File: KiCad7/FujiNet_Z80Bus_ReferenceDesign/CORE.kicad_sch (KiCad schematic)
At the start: 19 parts, among them IC1 74HC32N

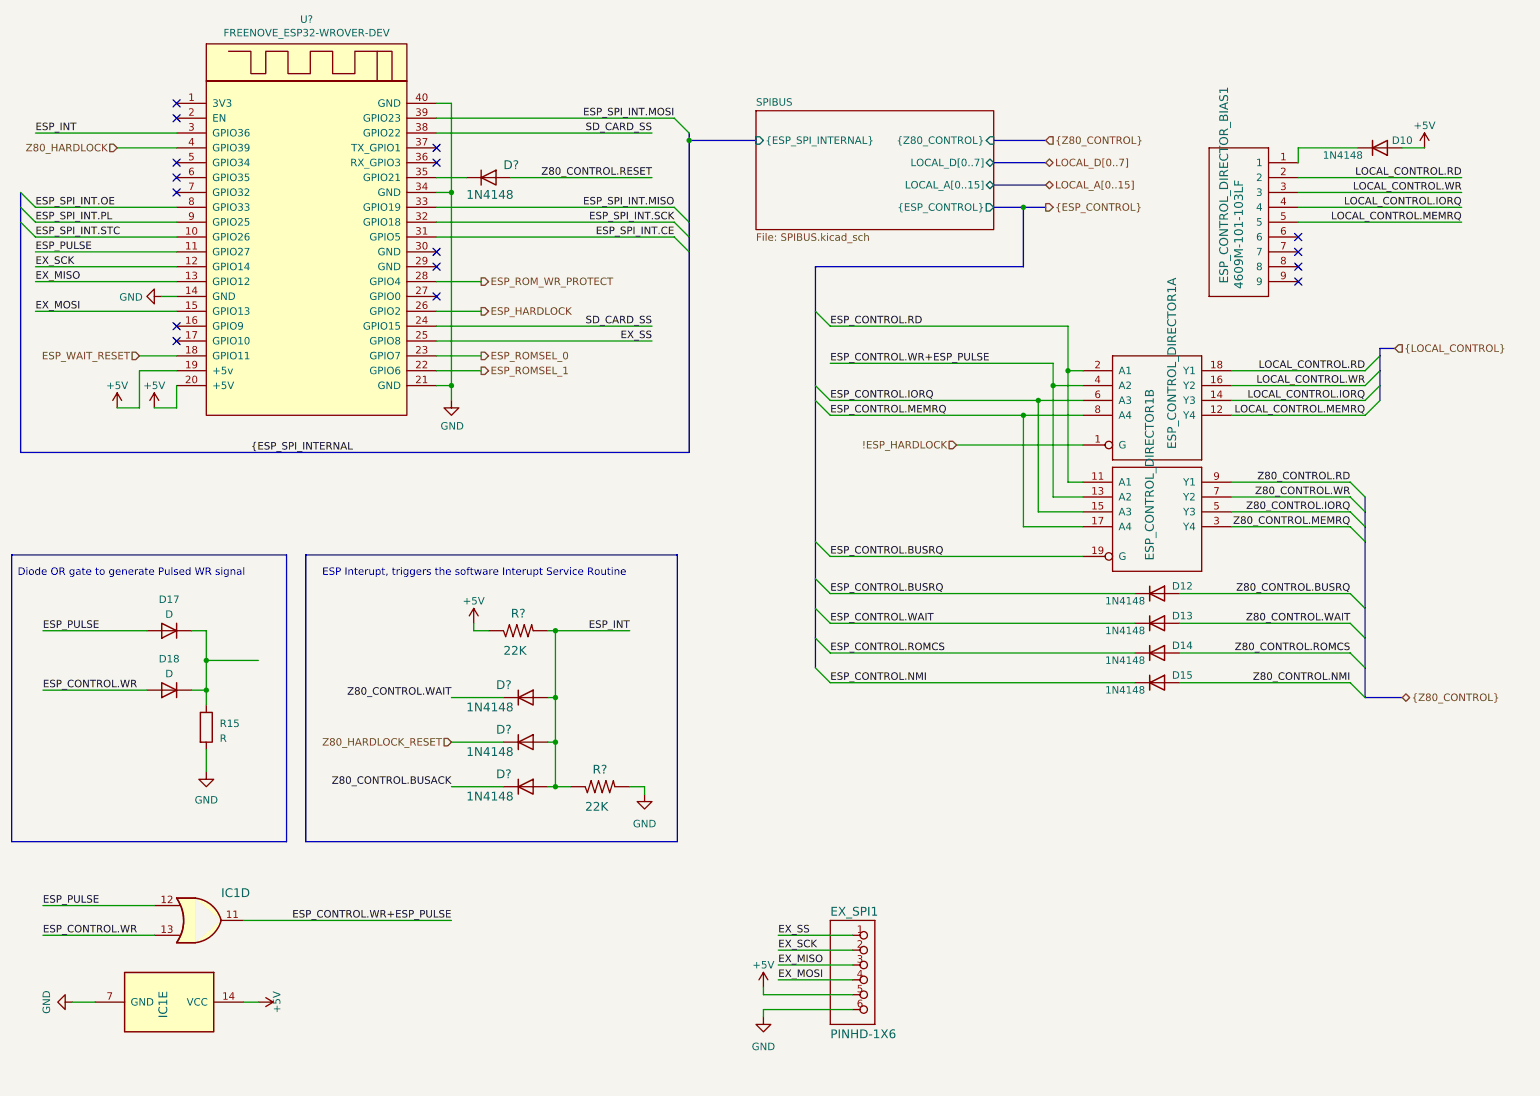
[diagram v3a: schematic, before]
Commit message: Kicad Symbols error fixes and ERC bug fixes
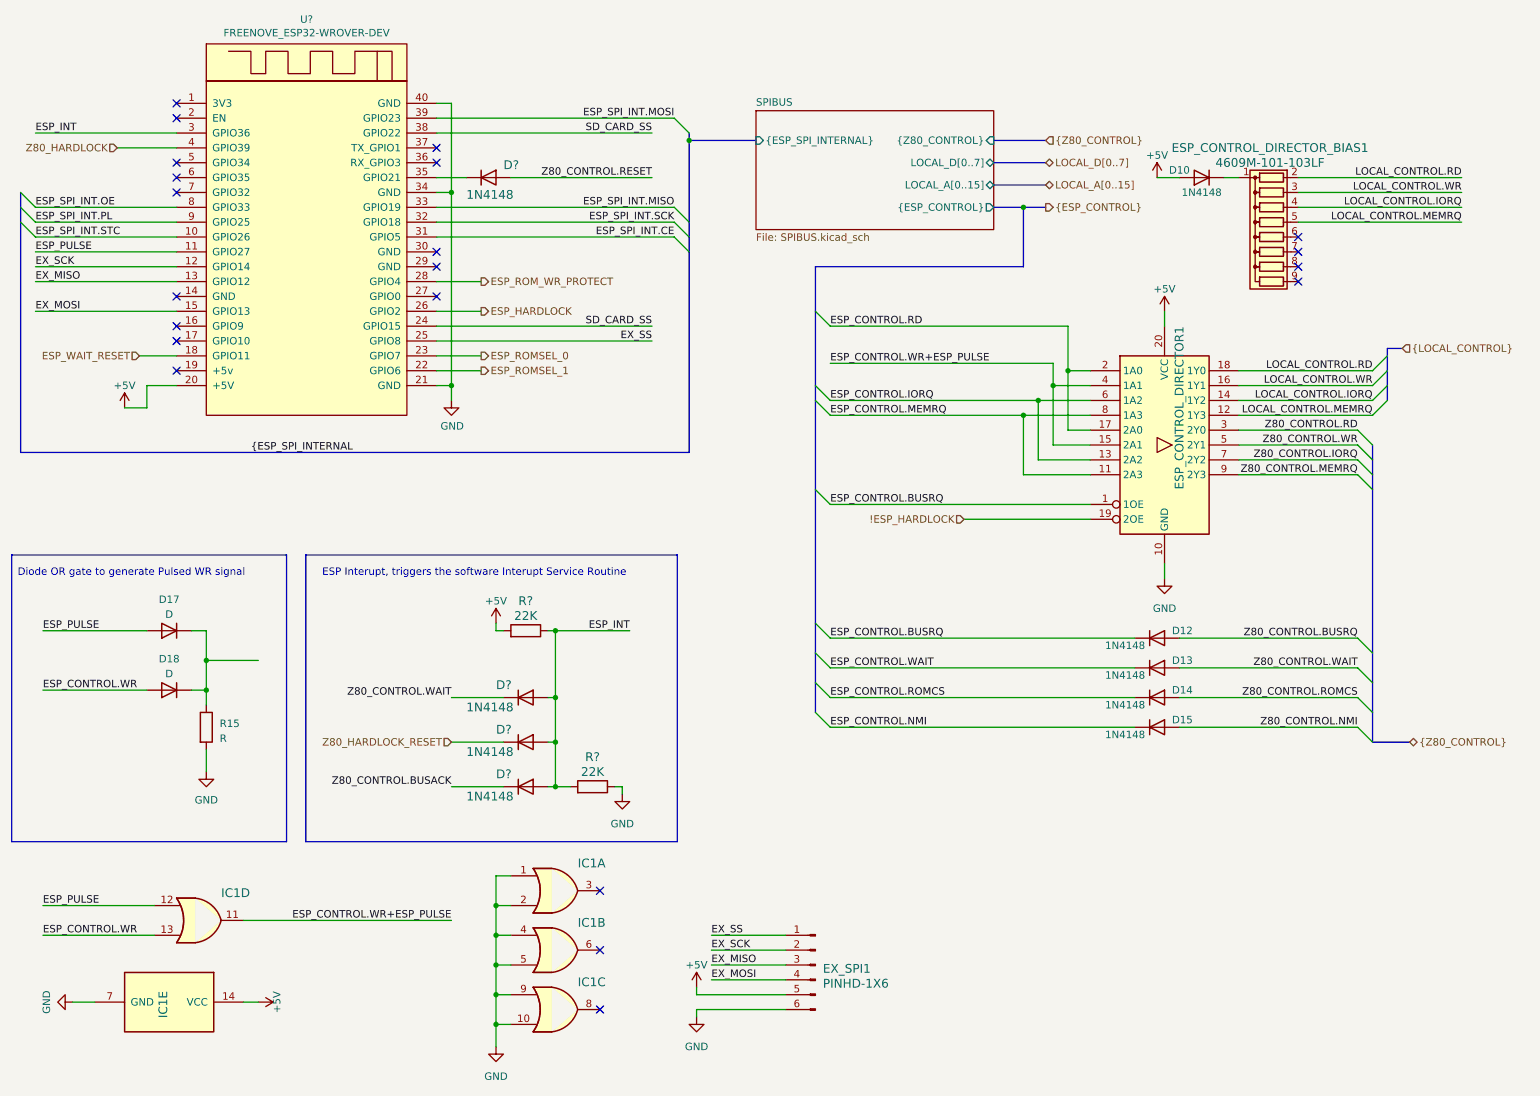
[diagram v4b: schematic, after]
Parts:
- removed unit 2 of ESP_CONTROL_DIRECTOR1
- added unit 1 of IC1
- added unit 2 of IC1
- added unit 3 of IC1
- ESP_CONTROL_DIRECTOR1: symbol FujiNet_Z80Bus_Reference-rescue:74244N-Z80ESP-eagle-import -> 74xx:74HC244
- ESP_CONTROL_DIRECTOR_BIAS1: symbol FujiNet_Z80Bus_Reference-rescue:4609M-101-103LF-Z80ESP-eagle-import -> Device:R_Network08
- EX_SPI1: symbol FujiNet_Z80Bus_Reference-rescue:PINHD-1X6-Z80ESP-eagle-import -> Connector:Conn_01x06_Pin
- R? (x2): symbol FujiNet_Z80Bus_Reference-rescue:R-US_0207_2V-Z80ESP-eagle-import -> Device:R
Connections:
- net !ESP_HARDLOCK: now also ESP_CONTROL_DIRECTOR1.19 (2OE); no longer ESP_CONTROL_DIRECTOR1.1 (G)
- net +5V: now also ESP_CONTROL_DIRECTOR1.20 (VCC), R?.2; no longer R?.1, U?.19 (+5v)
- net ESP_CONTROL.BUSRQ: now also ESP_CONTROL_DIRECTOR1.1 (1OE)
- net ESP_CONTROL.IORQ: now also ESP_CONTROL_DIRECTOR1.13 (2A2)
- net ESP_CONTROL.MEMRQ: now also ESP_CONTROL_DIRECTOR1.11 (2A3)
- net ESP_CONTROL.RD: now also ESP_CONTROL_DIRECTOR1.17 (2A0)
- net ESP_CONTROL.WR+ESP_PULSE: now also ESP_CONTROL_DIRECTOR1.15 (2A1)
- net ESP_INT: now also R?.1, R?.2; no longer R?.1, R?.2
- net GND: now also ESP_CONTROL_DIRECTOR1.10 (GND), R?.1, IC1.1, IC1.10, IC1.2, IC1.4, IC1.5, IC1.9; no longer R?.2, U?.14 (GND)
- net Z80_CONTROL.IORQ: now also ESP_CONTROL_DIRECTOR1.7 (2Y2)
- net Z80_CONTROL.MEMRQ: now also ESP_CONTROL_DIRECTOR1.9 (2Y3)
- net Z80_CONTROL.RD: now also ESP_CONTROL_DIRECTOR1.3 (2Y0)
- net Z80_CONTROL.WR: now also ESP_CONTROL_DIRECTOR1.5 (2Y1)
- no-connect marks 16 -> 21
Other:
- moved on the sheet: D10, D12, D13, D14, D15

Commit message: KiCad - ALMOST ERROR FREE!!!!
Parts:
- D17, D18: value D -> 1N4148
- EX_SPI1: value PINHD-1X6 -> PinSocket_2.54mm
- R15: value R -> R10K
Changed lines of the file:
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@@
       (effects (font (size 1.4986 1.4986)) (justify right))
     )
-    (property "Value" "PINHD-1X6" (at 156.21 179.705 0)
+    (property "Value" "PinSocket_2.54mm" (at 156.21 179.705 0)
       (effects (font (size 1.4986 1.4986)) (justify right))
     )
@@
       (effects (font (size 1.27 1.27)) (justify left))
     )
-    (property "Value" "R" (at 53.086 137.795 0)
+    (property "Value" "R10K" (at 53.086 137.795 0)
       (effects (font (size 1.27 1.27)) (justify left))
     )
@@
       (effects (font (size 1.27 1.27)))
     )
-    (property "Value" "D" (at 44.45 126.746 0)
+    (property "Value" "1N4148" (at 44.45 126.746 0)
       (effects (font (size 1.27 1.27)))
     )
@@
       (effects (font (size 1.27 1.27)))
     )
-    (property "Value" "D" (at 44.45 116.586 0)
-      (effects (font (size 1.27 1.27)))
-    )
+    (property "Value" "1N4148" (at 44.45 116.586 0)
+      (effects (font (size 1.27 1.27)))
+    )

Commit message: KiCAD PCB layout testing
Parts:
- D17, D18: footprint (none) -> Diode_THT:D_T-1_P5.08mm_Horizontal
- ESP_CONTROL_DIRECTOR1: value 74244N -> 74HC244N
- R15: footprint (none) -> Resistor_THT:R_Axial_DIN0207_L6.3mm_D2.5mm_P10.16mm_Horizontal
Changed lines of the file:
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@@
         )
         (path "/532c0392-800e-45cc-8170-6d32f2390e83/00000000-0000-0000-0000-000068f578e9"
-          (reference "U1") (unit 1)
+          (reference "ESP1") (unit 1)
         )
       )
@@
       (effects (font (size 1.4986 1.4986)))
     )
-    (property "Value" "74244N" (at 207.01 100.33 0)
+    (property "Value" "74HC244N" (at 207.01 100.33 0)
       (effects (font (size 1.4986 1.4986)) (justify left bottom) hide)
     )
@@
       (effects (font (size 1.27 1.27)) (justify left))
     )
-    (property "Footprint" "" (at 49.022 135.89 90)
+    (property "Footprint" "Resistor_THT:R_Axial_DIN0207_L6.3mm_D2.5mm_P10.16mm_Horizontal" (at 49.022 135.89 90)
       (effects (font (size 1.27 1.27)) hide)
     )
@@
       (effects (font (size 1.27 1.27)))
     )
-    (property "Footprint" "" (at 44.45 129.54 0)
+    (property "Footprint" "Diode_THT:D_T-1_P5.08mm_Horizontal" (at 44.45 129.54 0)
       (effects (font (size 1.27 1.27)) hide)
     )
@@
       (effects (font (size 1.27 1.27)))
     )
-    (property "Footprint" "" (at 44.45 119.38 0)
-      (effects (font (size 1.27 1.27)) hide)
-    )
+    (property "Footprint" "Diode_THT:D_T-1_P5.08mm_Horizontal" (at 44.45 119.38 0)
+      (effects (font (size 1.27 1.27)) hide)
+    )
